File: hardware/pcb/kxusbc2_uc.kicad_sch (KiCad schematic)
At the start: 19 parts, among them J2 UPDI, J6 Serial, SW1 SW_Push, U2 ATtiny3226-M, U4 RT9058-33GV, U5 LP5815DRLR, Y1 32.768 kHz

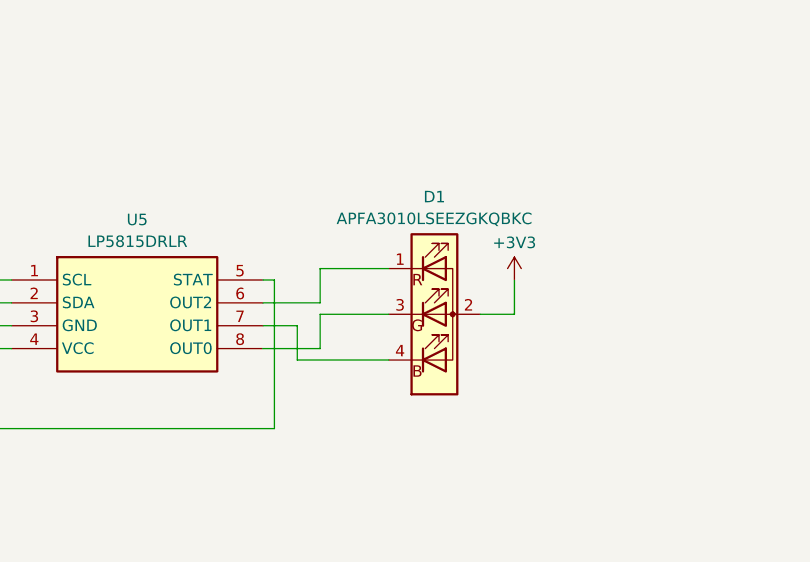
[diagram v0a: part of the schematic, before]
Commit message: Add new RGB LED and light pipe (closes #15)
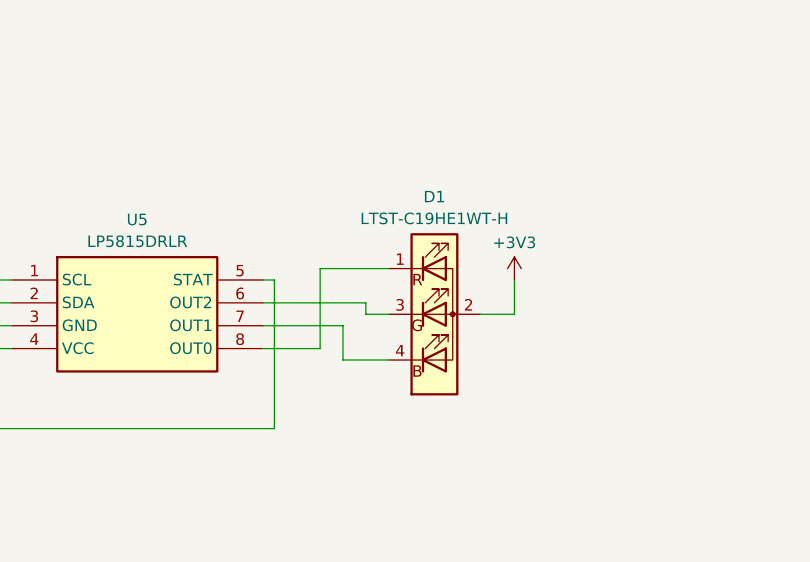
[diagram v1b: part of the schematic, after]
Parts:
- D1: value APFA3010LSEEZGKQBKC -> LTST-C19HE1WT-H; footprint LED_SMD:LED_Kingbright_APFA3010_3x1.5mm_Horizontal -> LED_SMD:LED_LiteOn_LTST-C19HE1WT; LCSC C5278712 -> C427425
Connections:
- net at U5.6 (OUT2): now also D1.3 (G); no longer D1.1 (R)
- net at U5.8 (OUT0): now also D1.1 (R); no longer D1.3 (G)
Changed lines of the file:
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@@
 		(comment 2 "© 2025 HB9DQM")
 	)
+	(rectangle
+		(start 242.57 130.81)
+		(end 242.57 130.81)
+		(stroke
+			(width 0)
+			(type default)
+		)
+		(fill
+			(type none)
+		)
+	)
 	(text "I2C addresses:\n0x22: FUSB302B\n0x2D: LP5815\n0x6B: BQ25792"
 		(exclude_from_sim no)
@@
 	(wire
 		(pts
-			(xy 198.12 153.67) (xy 208.28 153.67)
+			(xy 208.28 148.59) (xy 205.74 148.59)
+		)
+		(stroke
+			(width 0)
+			(type default)
+		)
+	)
+	(wire
+		(pts
+			(xy 205.74 147.32) (xy 194.31 147.32)
+		)
+		(stroke
+			(width 0)
+			(type default)
+		)
+	)
+	(wire
+		(pts
+			(xy 203.2 153.67) (xy 208.28 153.67)
 		)
 		(stroke
@@
 	(wire
 		(pts
-			(xy 194.31 149.86) (xy 198.12 149.86)
+			(xy 194.31 149.86) (xy 203.2 149.86)
 		)
 		(stroke
@@
 	(wire
 		(pts
-			(xy 200.66 148.59) (xy 208.28 148.59)
-		)
-		(stroke
-			(width 0)
-			(type default)
-		)
-	)
-	(wire
-		(pts
 			(xy 242.57 39.37) (xy 264.16 39.37)
 		)
@@
 	(wire
 		(pts
-			(xy 194.31 147.32) (xy 200.66 147.32)
-		)
-		(stroke
-			(width 0)
-			(type default)
-		)
-	)
-	(wire
-		(pts
 			(xy 128.27 45.72) (xy 130.81 45.72)
 		)
@@
 	(wire
 		(pts
-			(xy 194.31 152.4) (xy 200.66 152.4)
+			(xy 146.05 97.79) (xy 152.4 97.79)
 		)
 		(stroke
@@
 	(wire
 		(pts
-			(xy 146.05 97.79) (xy 152.4 97.79)
+			(xy 200.66 143.51) (xy 208.28 143.51)
 		)
 		(stroke
@@
 	(wire
 		(pts
-			(xy 200.66 152.4) (xy 200.66 148.59)
+			(xy 205.74 148.59) (xy 205.74 147.32)
 		)
 		(stroke
@@
 	(wire
 		(pts
-			(xy 198.12 149.86) (xy 198.12 153.67)
+			(xy 203.2 149.86) (xy 203.2 153.67)
 		)
 		(stroke
@@
 	(wire
 		(pts
-			(xy 149.86 106.68) (xy 149.86 109.22)
+			(xy 200.66 152.4) (xy 200.66 143.51)
 		)
 		(stroke
@@
 	(wire
 		(pts
-			(xy 146.05 62.23) (xy 137.16 62.23)
+			(xy 149.86 106.68) (xy 149.86 109.22)
 		)
 		(stroke
@@
 	(wire
 		(pts
-			(xy 99.06 113.03) (xy 99.06 116.84)
+			(xy 146.05 62.23) (xy 137.16 62.23)
 		)
 		(stroke
@@
 	(wire
 		(pts
-			(xy 267.97 39.37) (xy 267.97 36.83)
+			(xy 99.06 113.03) (xy 99.06 116.84)
 		)
 		(stroke
@@
 	(wire
 		(pts
-			(xy 73.66 62.23) (xy 73.66 64.77)
+			(xy 267.97 39.37) (xy 267.97 36.83)
 		)
 		(stroke
@@
 	(wire
 		(pts
-			(xy 251.46 67.31) (xy 264.16 67.31)
+			(xy 73.66 62.23) (xy 73.66 64.77)
 		)
 		(stroke
@@
 	(wire
 		(pts
-			(xy 200.66 143.51) (xy 208.28 143.51)
+			(xy 251.46 67.31) (xy 264.16 67.31)
 		)
 		(stroke
@@
 	(wire
 		(pts
-			(xy 152.4 161.29) (xy 160.02 161.29)
+			(xy 194.31 152.4) (xy 200.66 152.4)
 		)
 		(stroke
@@
 	(wire
 		(pts
-			(xy 195.58 161.29) (xy 160.02 161.29)
+			(xy 152.4 161.29) (xy 160.02 161.29)
 		)
 		(stroke
@@
 	(wire
 		(pts
-			(xy 73.66 72.39) (xy 73.66 73.66)
+			(xy 195.58 161.29) (xy 160.02 161.29)
 		)
 		(stroke
@@
 	(wire
 		(pts
-			(xy 129.54 118.11) (xy 139.7 118.11)
+			(xy 73.66 72.39) (xy 73.66 73.66)
 		)
 		(stroke
@@
 	(wire
 		(pts
-			(xy 116.84 72.39) (xy 114.3 72.39)
+			(xy 129.54 118.11) (xy 139.7 118.11)
 		)
 		(stroke
@@
 	(wire
 		(pts
-			(xy 149.86 116.84) (xy 149.86 118.11)
+			(xy 116.84 72.39) (xy 114.3 72.39)
 		)
 		(stroke
@@
 	(wire
 		(pts
-			(xy 129.54 48.26) (xy 129.54 50.8)
+			(xy 149.86 116.84) (xy 149.86 118.11)
 		)
 		(stroke
@@
 	(wire
 		(pts
-			(xy 200.66 147.32) (xy 200.66 143.51)
+			(xy 129.54 48.26) (xy 129.54 50.8)
 		)
 		(stroke
@@
 			)
 		)
-		(property "Value" "APFA3010LSEEZGKQBKC"
+		(property "Value" "LTST-C19HE1WT-H"
 			(at 213.36 137.9798 0)
 			(effects
@@
 			)
 		)
-		(property "Footprint" "LED_SMD:LED_Kingbright_APFA3010_3x1.5mm_Horizontal"
+		(property "Footprint" "LED_SMD:LED_LiteOn_LTST-C19HE1WT"
 			(at 213.36 135.89 0)
 			(effects
@@
 			)
 		)
-		(property "LCSC" "C5278712"
+		(property "LCSC" "C427425"
 			(at 213.36 148.59 0)
 			(effects
